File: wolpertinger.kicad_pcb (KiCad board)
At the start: 2 copper layers, 127.4 x 130.8 mm, 117 parts, among them J1 RIGHT IN, J2 LEFT IN, J3 EXT LFO, J4 LEFT OUT, J5 RIGHT OUT, J6 Jack-DC, K1 FRT5, K2 FRT5, Q1 BC549, Q2 BC547, Q3 BC547, SW1 ON/OFF, SW2 DPDT MONO/STEREO, SW3 DPDT HARMONIC/TREMOLO, U1 4093, U10 L78L05_TO92, U2 TL074, U3 TL074, U4 NE5532, U5 VTL5C, U6 VTL5C, U7 VTL5C, U8 VTL5C, U9 NE5532

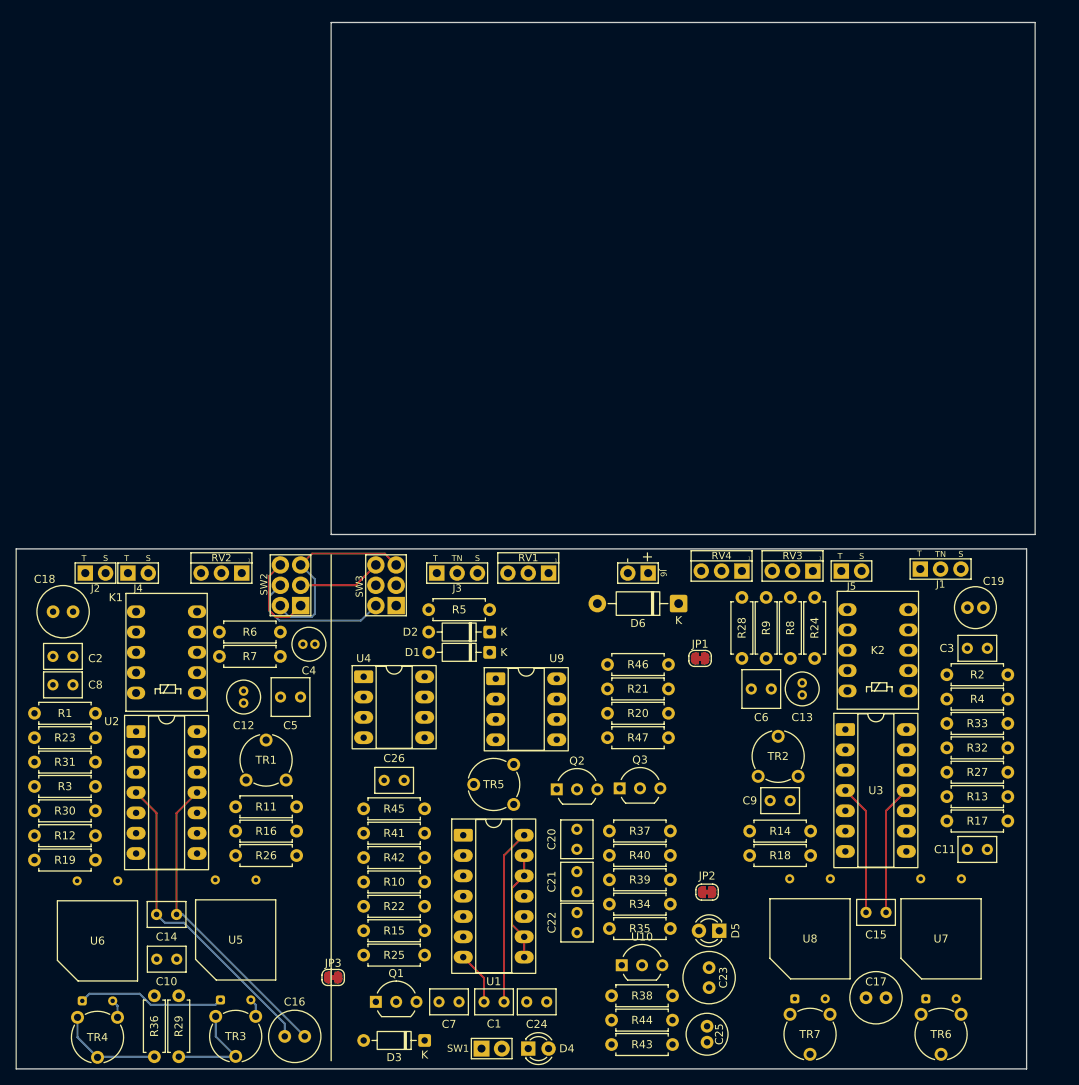
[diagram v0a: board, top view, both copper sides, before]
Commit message: minor position adjustments
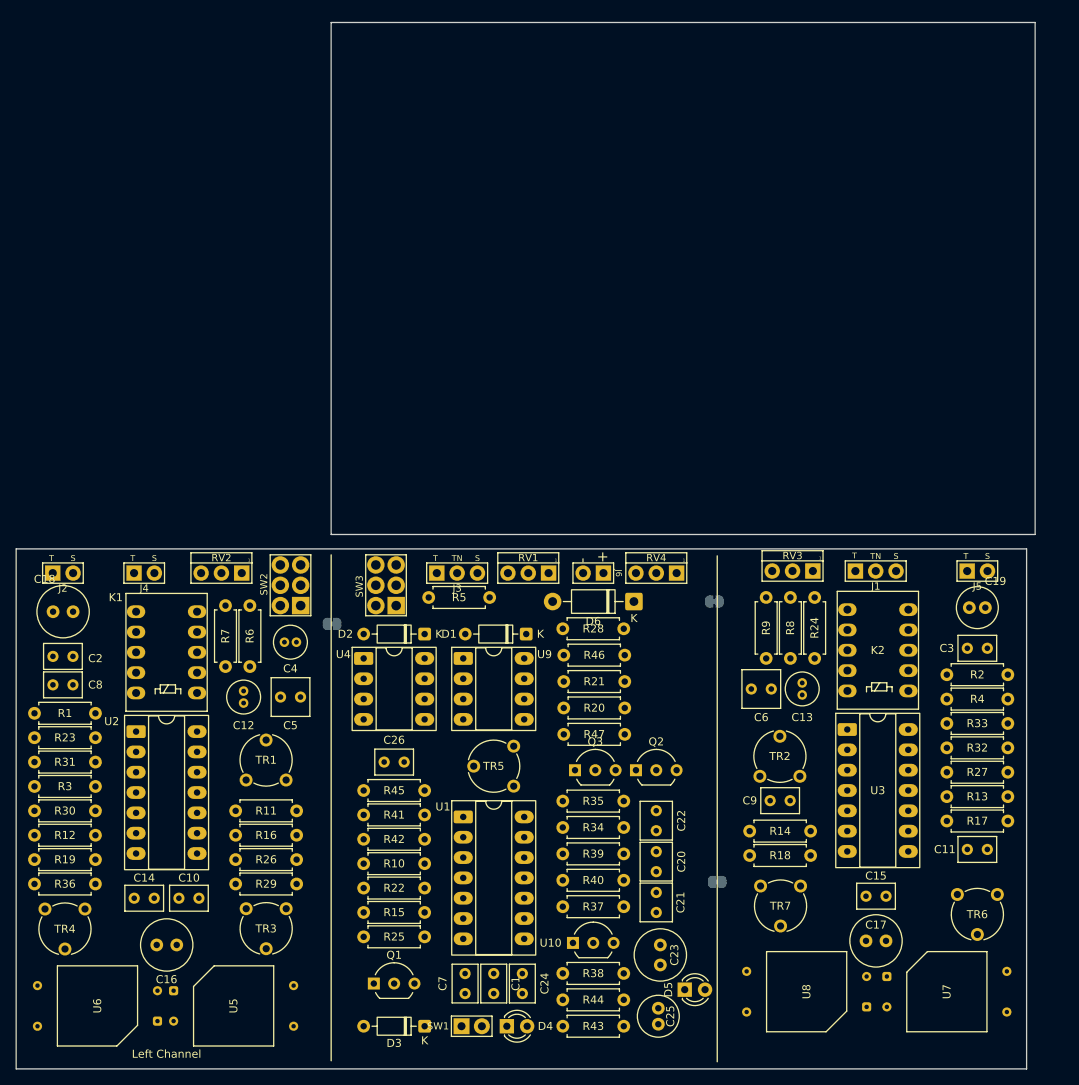
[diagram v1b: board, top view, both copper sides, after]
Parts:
- JP1, JP2, JP3: moved to B.Cu
- moved JP3 44.2 mm to (92.6, 73.7)
- moved JP2 36.3 mm to (140.4, 70.9)
- moved JP1 28.0 mm to (140.7, 105.9)
- moved R35 20.8 mm to (121.4, 95.8), turned to 0 degrees
- moved R29 20.3 mm to (88.1, 106.2), turned to 180 degrees
- moved C16 19.7 mm to (70.7, 113.8)
- moved C22 18.2 mm to (133.1, 97.0), turned to -90 degrees
- moved TR7 16.5 mm to (146.1, 106.4)
- moved R36 15.8 mm to (63.0, 106.2), turned to 180 degrees
- moved J5 15.7 mm to (173.2, 67.1)
- moved TR6 15.7 mm to (170.7, 107.5)
- moved R28 15.3 mm to (129.0, 74.3), turned to 180 degrees
- moved TR4 14.1 mm to (56.7, 109.3)
- moved TR3 14.0 mm to (81.8, 109.3)
- moved R40 13.8 mm to (121.4, 105.7), turned to 0 degrees
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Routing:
- net V1: track 39.6 -> 0.00 mm
- net GND1: track 38.6 -> 0.00 mm
- net LFO out: track 25.2 -> 0.00 mm
- net 9V: track 21.9 -> 0.00 mm
- net GND: track 20.6 -> 0.00 mm
- net GND3: track 18.5 -> 0.00 mm
- net Net-(SW2B-B): track 18.4 -> 0.00 mm
- net V2: track 16.3 -> 0.00 mm
- net GND2: track 16.3 -> 0.00 mm
- net Net-(R36-Pad2): track 13.2 -> 0.00 mm
- net Net-(R29-Pad2): track 13.2 -> 0.00 mm
- net LFO out inv: track 11.1 -> 0.00 mm
- net Net-(SW2A-B): track 10.5 -> 0.00 mm
- net hiL: track 2.31 -> 0.00 mm
- net loL: track 2.31 -> 0.00 mm
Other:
- board text added: "Left Channel"

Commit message: parts aligning pt1
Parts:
- moved R5 8.13 mm to (112.7, 71.3)
- moved U5 4.21 mm to (76.9, 118.5)
- moved R7 4.10 mm to (83.1, 69.9)
- moved R6 4.10 mm to (86.1, 69.9)
- moved C2 3.83 mm to (63.9, 76.9)
- moved C8 3.83 mm to (63.9, 80.5)
- moved J2 3.83 mm to (62.7, 66.5)
- moved C18 3.76 mm to (63.9, 71.6)
- moved C1 3.73 mm to (116.3, 116.1)
- moved C24 3.73 mm to (119.8, 116.1)
- moved C7 3.73 mm to (112.7, 116.1)
- moved K1 3.60 mm to (79.2, 81.5)
- moved TR4 3.60 mm to (60.2, 108.5)
- moved J6 3.58 mm to (128.7, 66.5)
- moved SW3 3.58 mm to (102.8, 68.0)
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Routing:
- net GND1: track 0.00 -> 96.2 mm
- net V1: track 0.00 -> 21.4 mm
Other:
- outline, holes or cut-outs redrawn
- board text added: "DEPTH"
- board text added: "DEPTH HIGH"
- board text added: "DEPTH LOW"
- board text added: "EXT. LFO"
- board text added: "GAIN"
- board text added: "HARMONIC/ CLASSIC"
- board text added: "IN"
- board text added: "LEFT CHANNEL"
- board text added: "LFO OFFSET"
- board text added: "MONO/STEREO"
- board text added: "OUT"
- board text added: "RIGHT CHANNEL"
- board text added: "SPEED"
- board text added: "STATUS"
- board text added: "SWITCH"
- board text added: "TONE"
- board text removed: "Left Channel"

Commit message: GND improvements
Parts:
- added JP1: ~, Jumper:SolderJumper-2_P1.3mm_Bridged_RoundedPad1.0x1.5mm, B.Cu at (109.5, 90.2)
- moved J4 1.21 mm to (71.4, 66.5)
- moved C12 1.09 mm to (84.2, 83.5)
- moved C4 1.00 mm to (89.6, 76.0)
- moved C5 0.85 mm to (91.6, 82.7)
- moved TR1 0.83 mm to (90.3, 93.2)
- moved SW2 0.48 mm to (90.4, 68.0)
- moved R7 0.40 mm to (82.7, 69.8)
- moved R6 0.40 mm to (85.7, 69.8)
- moved U5 0.25 mm to (77.1, 118.5)
- moved C18 0.22 mm to (63.9, 71.4)
- moved C2 0.21 mm to (63.9, 76.7)
- moved C10 0.14 mm to (76.8, 107.2)
- moved C16 0.13 mm to (74.0, 113.5)
- moved U2 0.13 mm to (71.4, 87.6)
- moved K1 0.13 mm to (79.1, 81.5)
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- renumbered C26 to C25, C25 to C26, JP1 to JP2, JP2 to JP3, JP3 to JP4, R39 to R38, R40 to R39, R38 to R40, R45 to R43, R46 to R44, R43 to R45, R44 to R46
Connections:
- C1 pad 2: GND -> GND4
- C23 pad 2: GND -> GND3
- C7 pad 2: GND -> GND4
- D5 pad 1: GND -> GND3
- Q1 pad 3: GND -> GND4
- U1 pad 12: GND -> GND4
- U1 pad 13: GND -> GND4
- U1 pad 7: GND -> GND4
- U1 pad 8: GND -> GND4
- U1 pad 9: GND -> GND4
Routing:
- net GND1: track 96.2 -> 0.00 mm
- net V1: track 21.4 -> 0.00 mm
